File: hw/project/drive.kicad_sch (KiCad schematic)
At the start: 45 parts, among them Q3 STL110N10F7, Q4 STL110N10F7, Q5 STL110N10F7, Q6 STL110N10F7, Q7 STL110N10F7, Q8 STL110N10F7

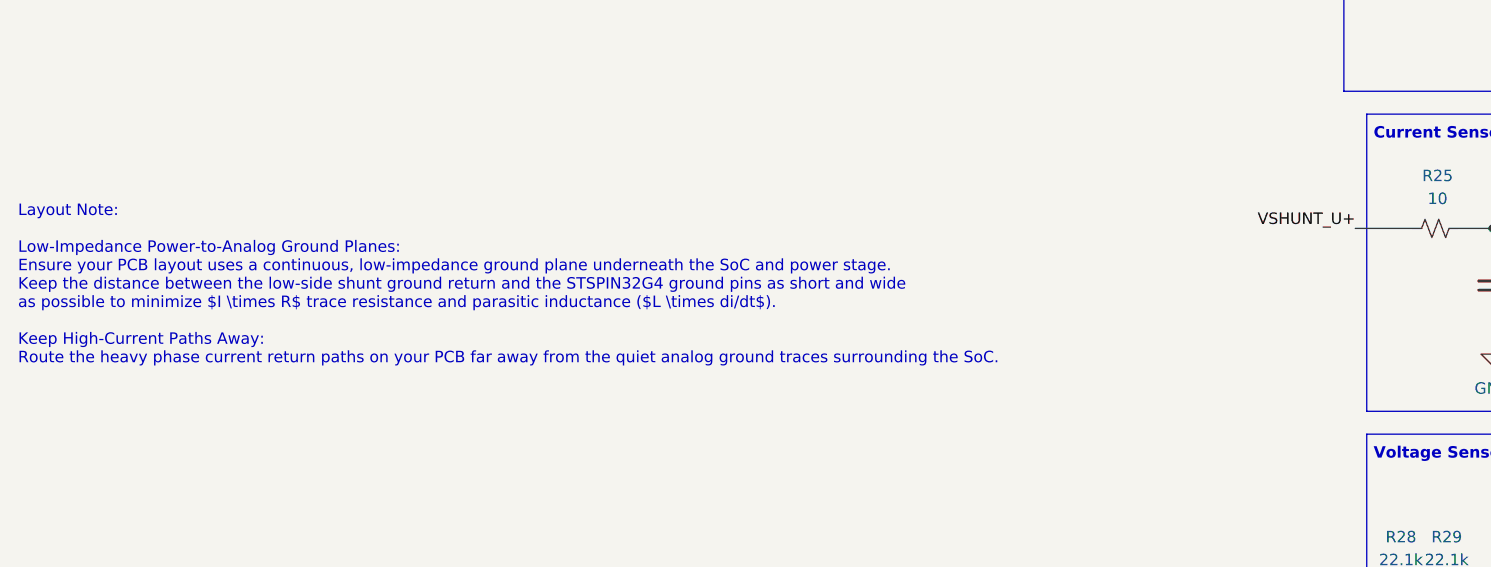
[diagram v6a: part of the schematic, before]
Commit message: Clean up before exporting gerbers
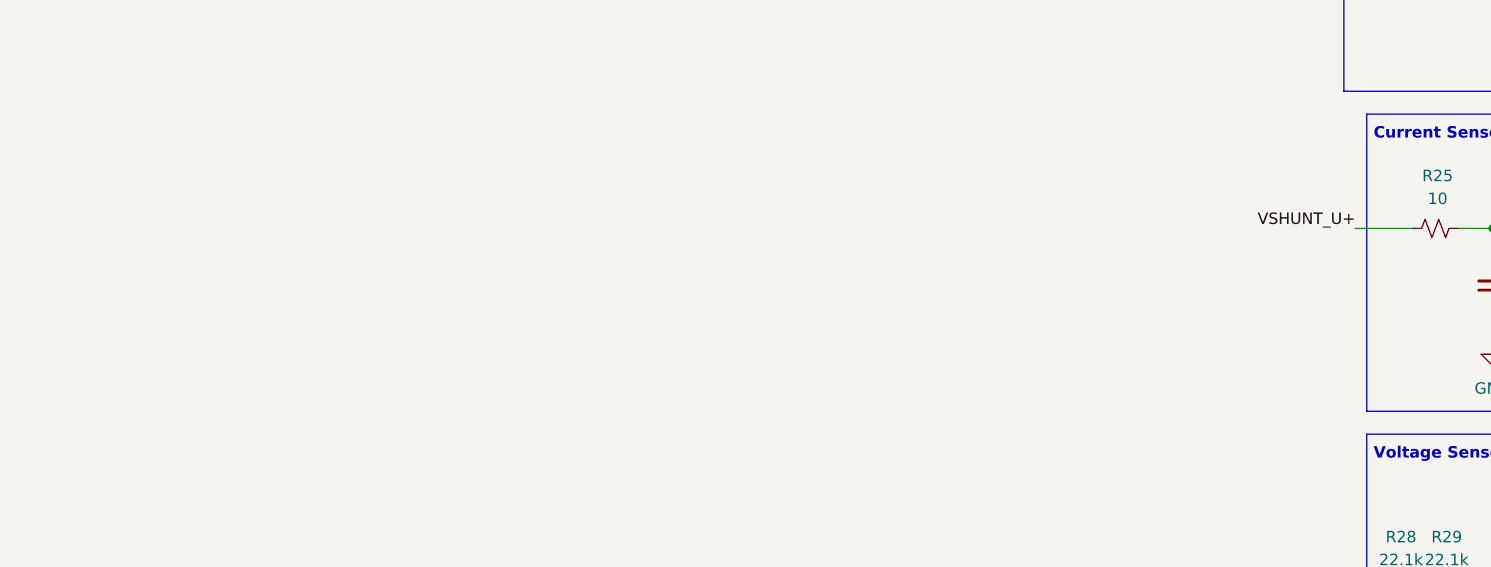
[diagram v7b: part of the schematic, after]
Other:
- note removed: "Layout Note: Low-Impedance Power-to-Analog Ground Planes: Ensure your PCB layout uses a continuous, low-impedance ground plane underneath the SoC and power stage. Keep the distance between the low-side shunt ground return and the STSPIN32G4 ground pins as short and wide as possible to minimize $I \times R$ trace resistance and parasitic inductance ($L \times di/dt$). Keep High-Current Paths Away: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"
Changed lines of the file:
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@@
-		)
-	)
-	(text "Layout Note: \n\nLow-Impedance Power-to-Analog Ground Planes: \nEnsure your PCB layout uses a continuous, low-impedance ground plane underneath the SoC and power stage. \nKeep the distance between the low-side shunt ground return and the STSPIN32G4 ground pins as short and wide \nas possible to minimize $I \\times R$ trace resistance and parasitic inductance ($L \\times di/dt$).\n\nKeep High-Current Paths Away: \nRoute the heavy phase current return paths on your PCB far away from the quiet analog ground traces surrounding the SoC."
-		(exclude_from_sim no)
-		(at -124.46 128.27 0)
-		(effects
-			(font
-				(size 1.27 1.27)
-				(color 255 4 4 1)
-			)
-			(justify left)
 		)
 	)
